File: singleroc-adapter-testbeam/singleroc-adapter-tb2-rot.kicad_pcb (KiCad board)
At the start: 2 copper layers, 64 x 73.8 mm, 33 parts

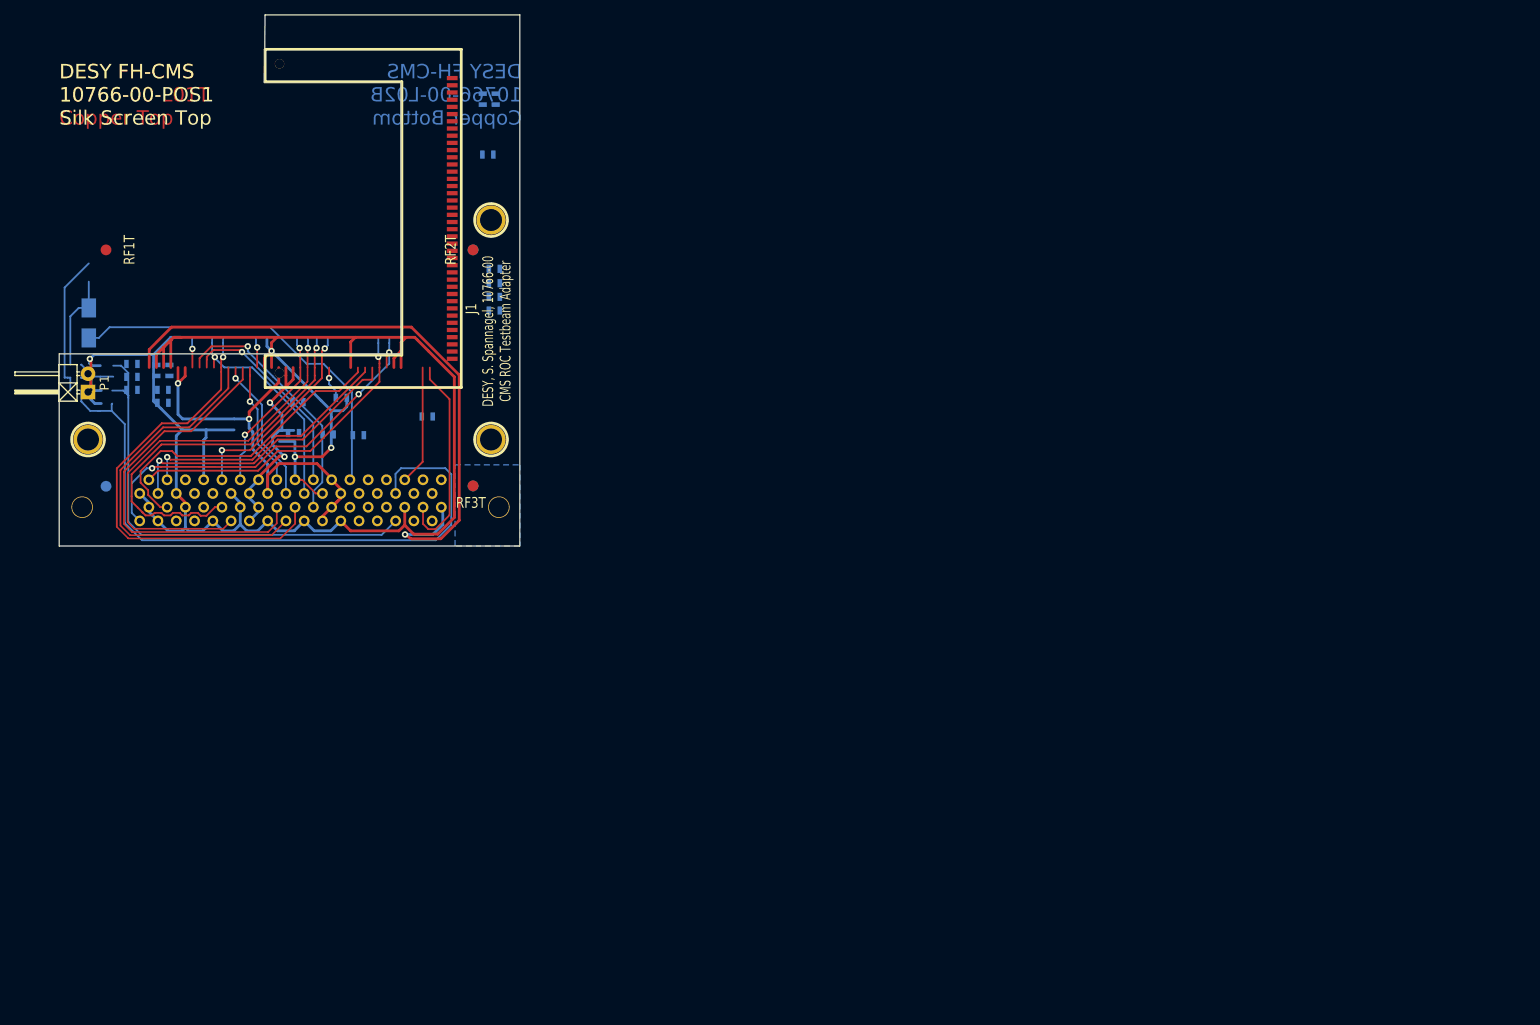
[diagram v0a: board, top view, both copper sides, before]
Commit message: Rotatted adapter routed in principle. Space issues observed, need to try another approach (maybe add some space). Learned that the edge connector should be rotated the other way round - will start another PCB
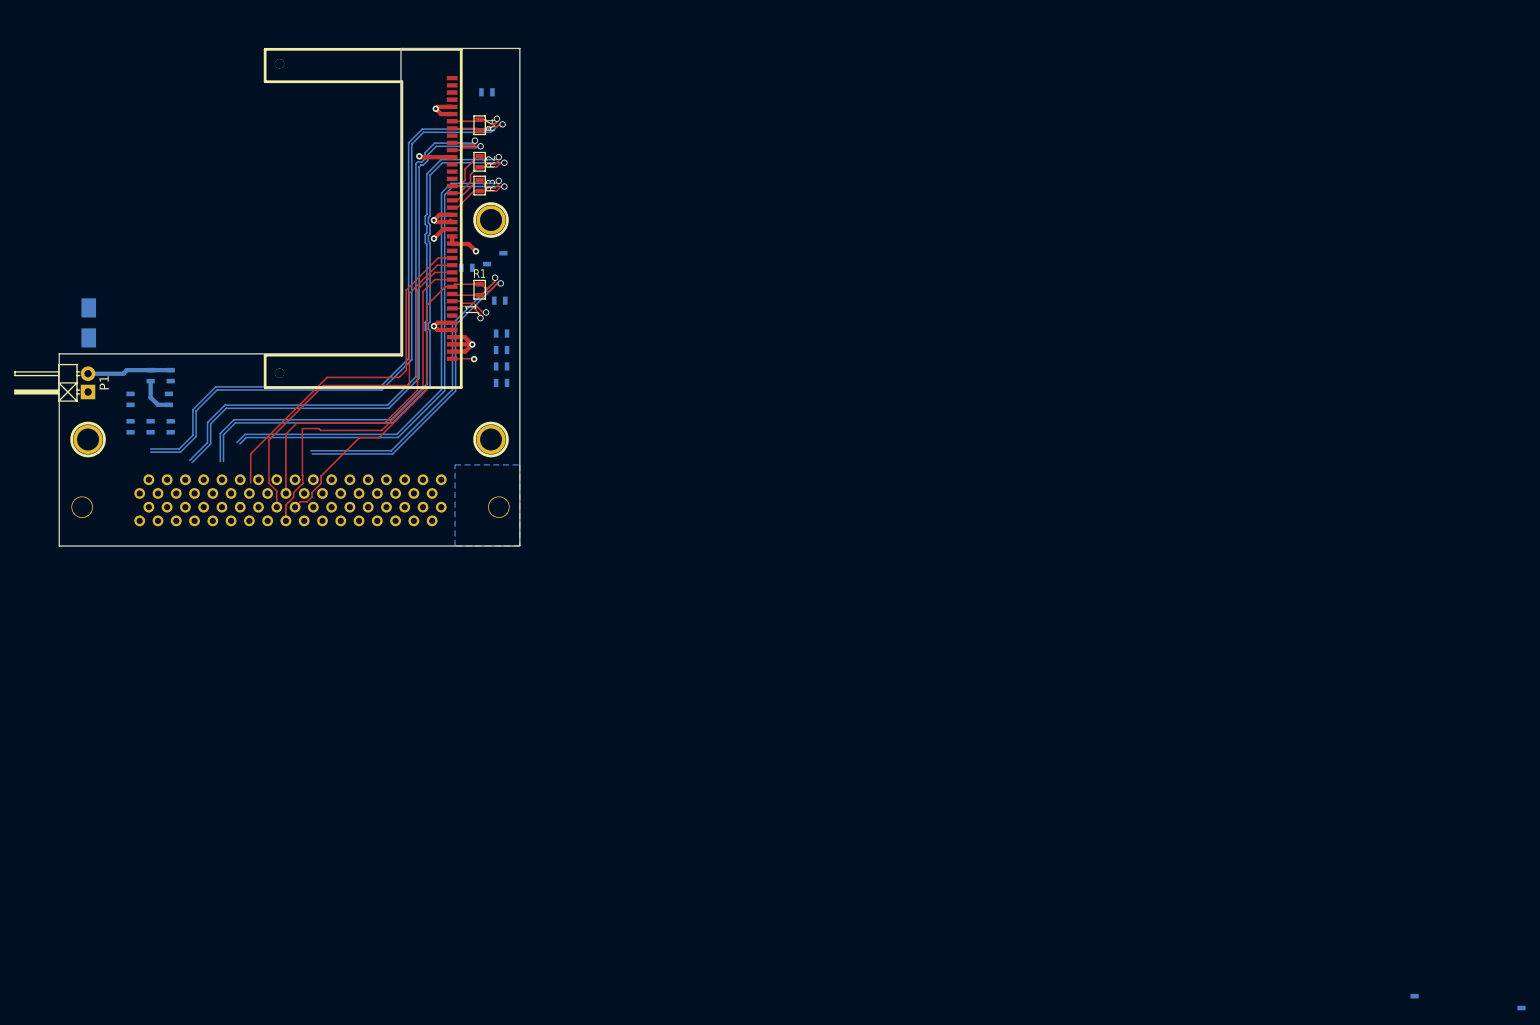
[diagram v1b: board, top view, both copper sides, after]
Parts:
- removed RF1B, RF1T, RF2B, RF2T, RF3B, RF3T: , Connect:1pin
- R1, R2, R3, R4: moved to F.Cu
- moved C3 47.0 mm to (146.4, 55.8)
- moved R4 46.3 mm to (145.4, 60.3), turned to 270 degrees
- moved R2 43.4 mm to (145.4, 65.4), turned to 270 degrees
- moved R3 43.0 mm to (145.4, 68.7), turned to 270 degrees
- moved C2 30.0 mm to (143.6, 80.1)
- moved C4 22.4 mm to (148.7, 78.9)
- moved C6 22.2 mm to (146.4, 78.9)
- moved C1 20.4 mm to (148.2, 84.7)
- moved R1 19.1 mm to (145.4, 83.2), turned to 270 degrees
- moved C7 12.0 mm to (148.5, 96.1)
- moved C8 11.6 mm to (148.5, 93.9)
- moved C9 11.3 mm to (148.5, 91.6)
- moved R9 8.62 mm to (96.9, 102.2), turned to 270 degrees
- moved R6 8.26 mm to (99.7, 102.2), turned to 90 degrees
- moved R5 5.74 mm to (102.5, 95.1), turned to 90 degrees
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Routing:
- net GND: track 263.5 -> 28.8 mm, vias 5 -> 4
- net AIN0: track 89.1 -> 0.00 mm
- net AIN1: track 64.4 -> 0.00 mm
- net HV: track 87.1 -> 25.8 mm
- net CTR+: track 28.2 -> 86.4 mm, vias 2 -> 1
- net Net-(F1-Pad2): track 53.2 -> 0.00 mm
- net CLK-: track 23.5 -> 76.0 mm, vias 2 -> 1
- net TIN-: track 43.9 -> 94.9 mm
- net SOUT+: track 36.4 -> 81.4 mm
- net RESET: track 40.9 -> 0.00 mm, vias 1 -> 0
- net TIN+: track 54.3 -> 94.1 mm, vias 3 -> 1
- net SOUT-: track 44.2 -> 81.8 mm, vias 0 -> 1
- net VA: track 33.5 -> 67.8 mm, vias 2 -> 1
- net I2C_A3: track 17.1 -> 49.9 mm, vias 1 -> 0
- net TOUT-: track 35.8 -> 5.00 mm
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- added copper zone on In2.Cu, net GND
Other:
- board size 64 x 73.8 mm -> 64 x 69.1 mm
- copper layers 2 -> 4
- net class Power added: clearance 0.22, trace_width 0.5, via_dia 0.889, via_drill 0.635
- board text added: "This leg og the edge connector needs to be cut away in order to fit into the DUT box"
- board text removed: "DESY FH-CMS 10766-00-BOHR Drill Map"
- board text removed: "DESY FH-CMS 10766-00-L01T Copper Top"
- board text removed: "DESY FH-CMS 10766-00-L02B Copper Bottom"
- board text removed: "DESY FH-CMS 10766-00-LSM1 Solder Resist Top"
- board text removed: "DESY FH-CMS 10766-00-LSM2 Solder Resist Bottom"
- board text removed: "DESY FH-CMS 10766-00-POS1 Silk Screen Top"
- board text removed: "DESY FH-CMS 10766-00-POS2 Silk Screen Bottom"
- board text removed: "DESY FH-CMS 10766-00-SMD1 Solder Paste Top"
- board text removed: "DESY FH-CMS 10766-00-SMD2 Solder Paste Bottom"
- board text removed: "DESY, S. Spannagel, 10766-00 CMS ROC Testbeam Adapter"
